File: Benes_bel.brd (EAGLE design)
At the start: 82.5 x 67.3 mm, 27 parts, among them J1 DCJ0202, K1 HE751, K2 HE751, K3 HE751, K4 HE751, T1 BC337, T2 BC337, T3 BC337, T4 BC337, X5 FH12-08S-1SH

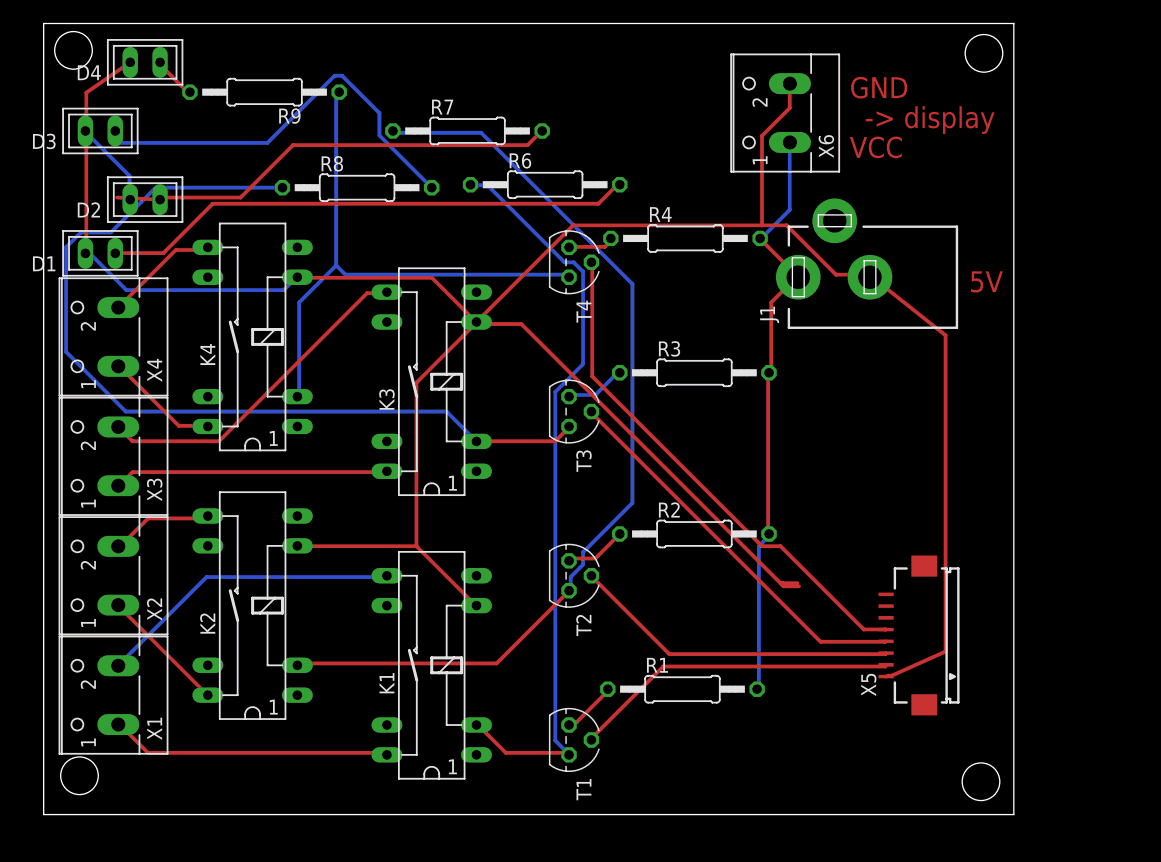
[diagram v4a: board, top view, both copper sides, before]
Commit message: met high level switch + speaker + mic
eerste versie was met een low level switch
nu met met darlington (npn+pnp)
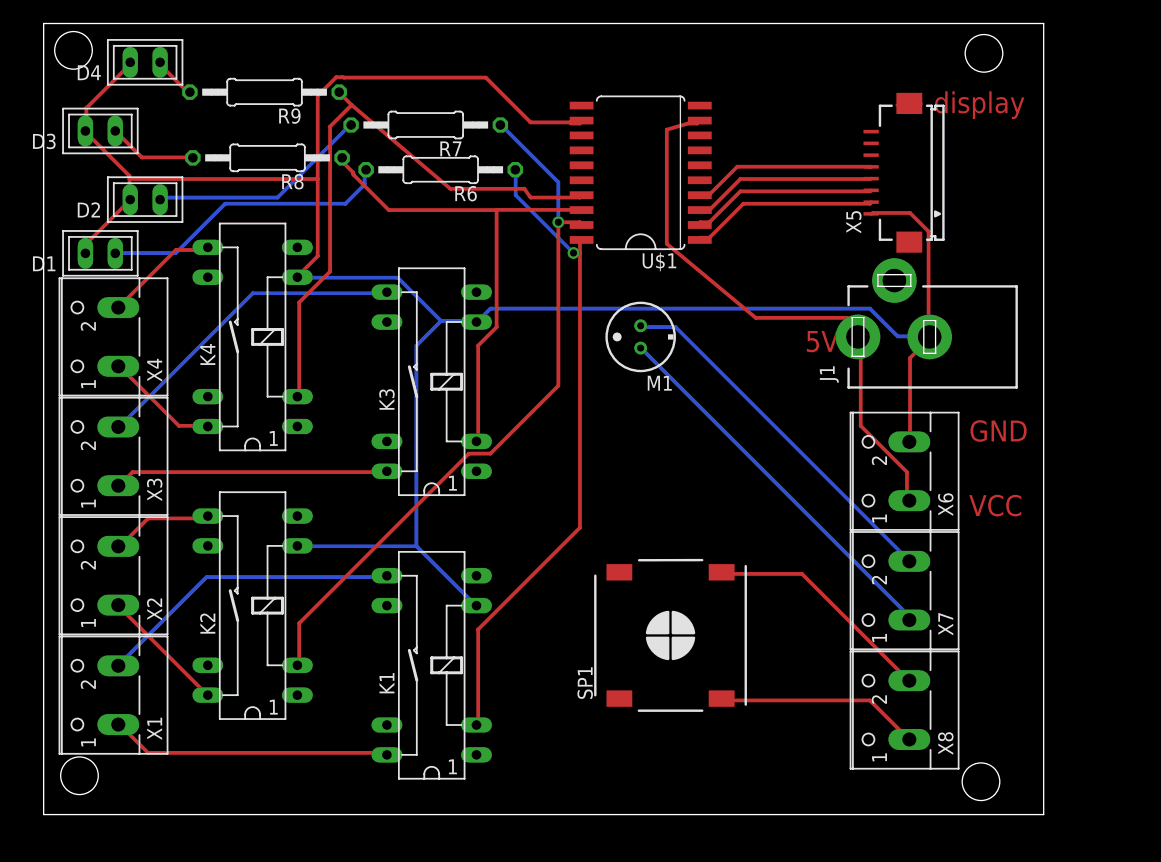
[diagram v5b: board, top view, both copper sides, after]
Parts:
- removed R1, R2, R3, R4: (no value), resistor:0207/12
- removed T1, T2, T3, T4: BC337, transistor:TO92
- added M1: ELECTRET_MICROPHON-WM-61B, microphon:WM-61B
- added SP1: SMS-1308MS-2-R, speaker:SMS-1308MS-2-R
- added U$1: A2982SSO20WA2982, gxb:SO20W
- added X7, X8: (no value), con-wago-500:W237-102
- moved X5 39.4 mm to (72.4, 54.6)
- moved X6 32.1 mm to (71.1, 29.2)
- moved R6 8.98 mm to (32.5, 54.9), turned to 180 degrees
- moved R8 8.03 mm to (17.8, 55.9), turned to 180 degrees
- moved J1 7.18 mm to (71.1, 40.6)
- moved R7 3.59 mm to (31.2, 58.7), turned to 180 degrees
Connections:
- removed net N$10: T4.2, X5.5
- new net N$22: J1.1, U$1.9, X6.1
- net N$1: now also U$1.1, X5.2; no longer R1.1, T1.3
- net N$19: now also U$1.18; no longer T3.1
- net N$2: now also U$1.2, X5.3; no longer R2.1, T2.3
- net N$20: now also U$1.17; no longer T4.1
- net N$21: now also U$1.12
- net N$23: now also U$1.20; no longer T1.1
- net N$3: now also U$1.3, X5.4; no longer R3.1, T3.3
- net N$4: now also U$1.4, X5.5; no longer R4.1, T4.3
- net N$5: now also U$1.19; no longer T2.1
- net N$6: now also SP1.+, X8.1; no longer J1.1, R1.2, R2.2, R3.2, R4.2, X6.1
- net N$7: now also SP1.-, X8.2; no longer T1.2, X5.2
- net N$8: now also M1.1, X7.1; no longer T2.2, X5.3
- net N$9: now also M1.2, X7.2; no longer T3.2, X5.4
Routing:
- net N$22: track 0.00 -> 48.2 mm
- net N$10: track 43.7 -> 0.00 mm
- net N$21: track 233.8 -> 197.3 mm
- net N$6: track 51.2 -> 17.5 mm
- net N$19: track 75.9 -> 43.2 mm
- net N$27: track 35.1 -> 7.54 mm
- net N$25: track 45.3 -> 24.9 mm
- net N$26: track 38.7 -> 18.9 mm
- net N$5: track 79.9 -> 60.4 mm, vias 0 -> 1
- net N$4: track 3.97 -> 15.6 mm
- net N$1: track 4.70 -> 16.0 mm
- net N$2: track 5.29 -> 15.9 mm
- net N$3: track 5.14 -> 15.7 mm
- net N$23: track 64.1 -> 54.7 mm, vias 0 -> 1
- net N$7: track 27.8 -> 19.8 mm
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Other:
- board size 82.5 x 67.3 mm -> 85.1 x 67.3 mm
